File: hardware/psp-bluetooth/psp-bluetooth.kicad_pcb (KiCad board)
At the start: 2 copper layers, 45.7 x 73.7 mm, 16 parts, among them J1 Left Connector, J2 Center Connector, J3 Right Connector, J4 Analog Connector, J5 PSP Power out, J6 Power IN, J7 Serial, J8 Vin Toggle, P1 Digital, P2 Analog, P3 CONN_01X01, P4 CONN_01X01, P5 CONN_01X01, P6 CONN_01X01, U1 MCP4251-xxxx-P

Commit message: Final
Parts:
- added JP1: SJ Vin Toggle, Jumper:SolderJumper-2_P1.3mm_Open_Pad1.0x1.5mm, F.Cu at (148.0, 64.1)
- added SW1: SW_Push, Button_Switch_SMD:SW_Push_1P1T_NO_6x6mm_H9.5mm, F.Cu at (120.7, 92.7)
- J6: value Power IN -> Barrel_Jack; footprint Connector_PinHeader_2.54mm:PinHeader_1x02_P2.54mm_Vertical -> Connector_BarrelJack:BarrelJack_CUI_PJ-063AH_Horizontal
- moved J7 22.5 mm to (133.3, 71.1)
- moved J5 18.5 mm to (134.0, 64.1), turned to -90 degrees
- moved S1 6.54 mm to (142.9, 54.5)
- moved J6 4.28 mm to (125.1, 58.8), turned to 180 degrees
- moved J8 4.07 mm to (152.4, 64.1), turned to 90 degrees
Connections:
- net Net-(J4-Pad2) renamed /P1W
- net Net-(J4-Pad3) renamed /P0A/P1A
- net Net-(J4-Pad4) renamed /P0W
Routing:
- net /A6 (D20): track 0.00 -> 40.7 mm
- net /1(Tx): track 33.4 -> 6.15 mm
- net /0(Rx): track 33.4 -> 6.15 mm
- net Net-(J5-Pad2): track 22.3 -> 42.3 mm
- net VIN: track 7.86 -> 16.9 mm
- net Net-(J6-Pad2): track 8.17 -> 15.9 mm
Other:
- board text added: "+ -"
- board text added: "Arduino Nano 33 IOT"
- board text added: "Centre Connector"
- board text added: "Controller Sync"
- board text added: "Left Connector"
- board text added: "MCP4251"
- board text added: "PSP Bluetooth Consolizer V2.5 Stephen Cooper 2022"
- board text added: "Right Connector"
- board text added: "usb"
- board text removed: "GND"
- board text removed: "PSP Bluetooth Consolizer V2 Stephen Cooper 2022"
- board text removed: "Power"
- board text removed: "rx"
- board text removed: "tx"

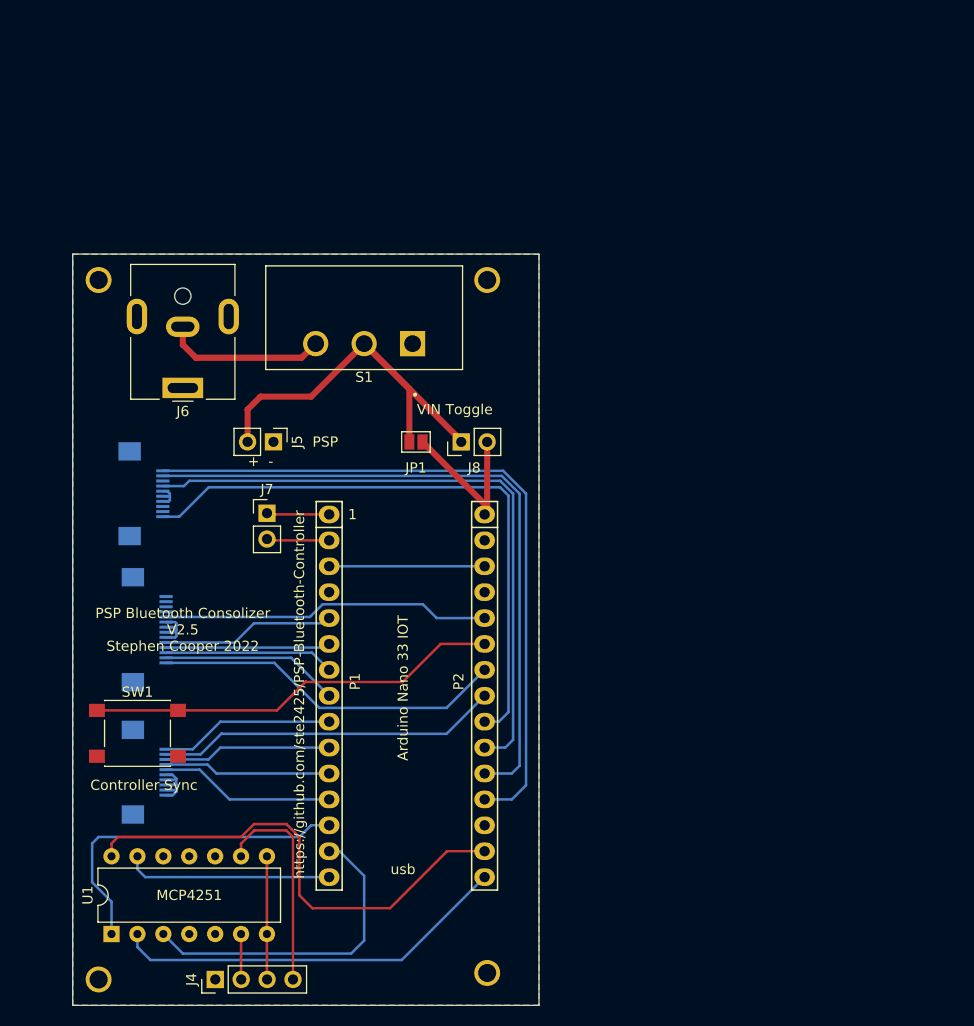
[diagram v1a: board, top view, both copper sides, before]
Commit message: Made kicad project portable and finished V1.
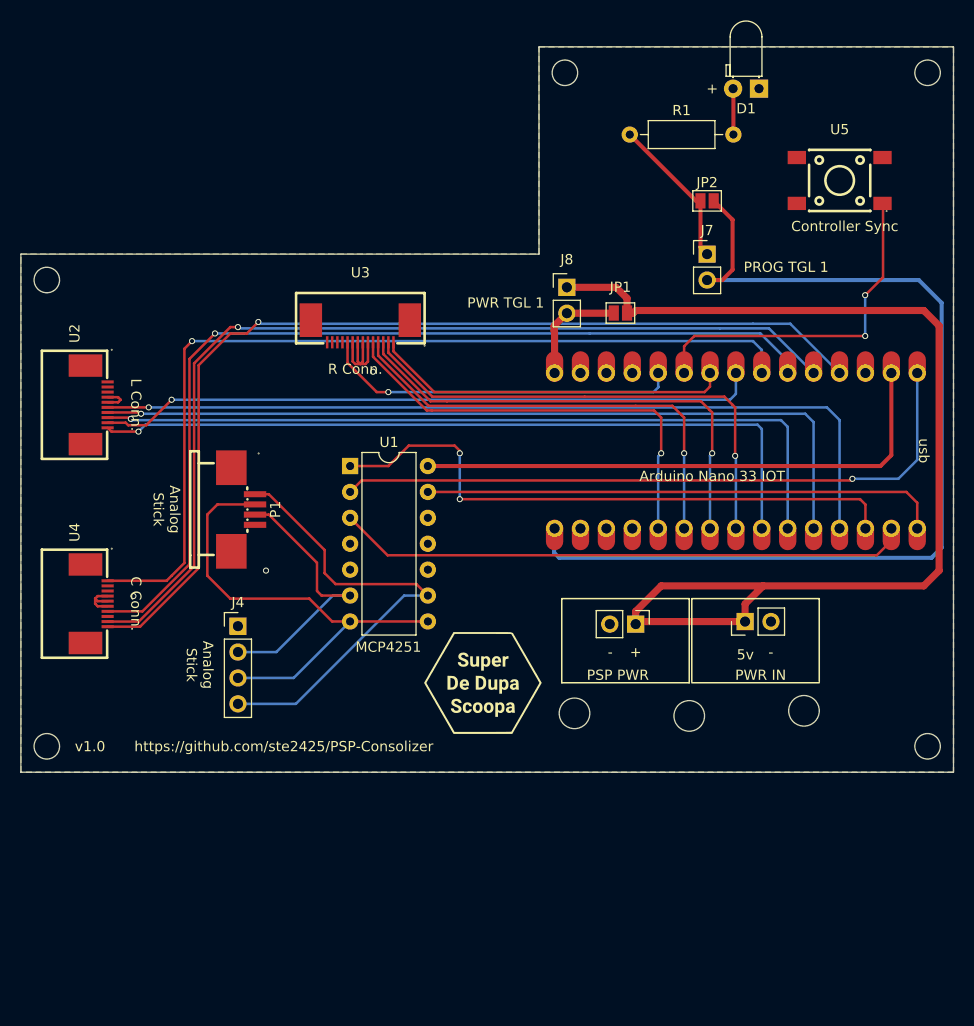
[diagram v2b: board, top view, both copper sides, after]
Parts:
- removed J5: PSP Power out, Connector_PinHeader_2.54mm:PinHeader_1x02_P2.54mm_Vertical
- removed J6: Barrel_Jack, Connector_BarrelJack:BarrelJack_CUI_PJ-063AH_Horizontal
- removed P2: Analog, Socket_Arduino_Nano:Socket_Strip_Arduino_1x15
- removed P3, P4, P5, P6: CONN_01X01, Socket_Arduino_Nano:1pin_Nano
- removed S1: L102021ML04Q, L102021ML04Q:SW_L102021ML04Q
- removed SW1: SW_Push, Button_Switch_SMD:SW_Push_1P1T_NO_6x6mm_H9.5mm
- added D1: LED, LED_THT:LED_D3.0mm_Horizontal_O1.27mm_Z6.0mm, F.Cu at (181.6, 29.5)
- added G***: LOGO, Graphics:pcblogo, F.Cu at (154.5, 87.8)
- added H1: MountingHole, MountingHole:MountingHole_2.5mm, F.Cu at (162.6, 27.9)
- added H2: MountingHole, MountingHole:MountingHole_2.5mm, F.Cu at (198.1, 27.9)
- added H3: MountingHole, MountingHole:MountingHole_2.5mm, F.Cu at (198.1, 94.0)
- added H4: MountingHole, MountingHole:MountingHole_2.5mm, F.Cu at (111.8, 94.0)
- added H5: MountingHole, MountingHole:MountingHole_2.5mm, F.Cu at (111.8, 48.3)
- added JP2: SJ LED Indicator, Jumper:SolderJumper-2_P1.3mm_Open_Pad1.0x1.5mm, F.Cu at (176.5, 40.5)
- added R1: 140 ohm, Resistor_THT:R_Axial_DIN0207_L6.3mm_D2.5mm_P10.16mm_Horizontal, F.Cu at (168.9, 34.0)
- added REF**: MountingHole_3mm, MountingHole:MountingHole_3mm, F.Cu at (174.8, 91.0)
- added REF**: MountingHole_3mm, MountingHole:MountingHole_3mm, F.Cu at (186.0, 90.5)
- added REF**: MountingHole_3mm, MountingHole:MountingHole_3mm, F.Cu at (163.5, 90.8)
- added U2: AFC07-S10ECA-00, JLCPCB_footprint:FPC-SMD_P0.50-10P_LCS-SJ-H2.0, F.Cu at (114.5, 60.5)
- added U3: AFC07-S14ECA-00, JLCPCB_footprint:FPC-SMD_P0.50-14P_LCS-SJ-H2.0, F.Cu at (142.5, 52.0)
- added U4: AFC07-S10ECA-00, JLCPCB_footprint:FPC-SMD_P0.50-10P_LCS-SJ-H2.0, F.Cu at (114.5, 80.0)
- added U5: TS-1102SD-A-F-R, JLCPCB_footprint:SW-SMD_4P-L6.0-W6.0-P4.50-LS9.2, F.Cu at (189.5, 38.5)
- J1: value Left Connector -> Arduino-NANO-33; footprint Connector_FFC-FPC:Hirose_FH12-10S-0.5SH_1x10-1MP_P0.50mm_Horizontal -> Nano_33:NANO_33_Socket_Castell&SMD; moved to F.Cu
- J2: value Center Connector -> Conn_01x02; footprint Connector_FFC-FPC:Hirose_FH12-10S-0.5SH_1x10-1MP_P0.50mm_Horizontal -> Connector_PinHeader_2.54mm:PinHeader_1x02_P2.54mm_Vertical; moved to F.Cu
- J3: value Right Connector -> Conn_01x02; footprint Connector_FFC-FPC:Hirose_FH12-14S-0.5SH_1x14-1MP_P0.50mm_Horizontal -> Connector_PinHeader_2.54mm:PinHeader_1x02_P2.54mm_Vertical; moved to F.Cu
- J7: value Serial -> Programming Header 1
- P1: value Digital -> FPC_4P_Pull_type_1_0MM_Under_the_next; footprint Socket_Arduino_Nano:Socket_Strip_Arduino_1x15 -> JLCPCB_footprint:FPC-SMD_AFA07-S04FCC-00
- moved J1 65.8 mm to (179.3, 65.0), turned to 180 degrees
- moved J3 58.6 mm to (180.2, 81.8)
- moved U1 51.5 mm to (141.5, 66.5), turned to 0 degrees
- moved J7 50.1 mm to (176.5, 45.7)
- moved J2 49.9 mm to (169.5, 82.0), turned to -90 degrees
- moved J4 34.7 mm to (130.5, 82.2), turned to 0 degrees
- moved JP1 23.7 mm to (168.0, 51.5), turned to 180 degrees
- moved J8 18.4 mm to (162.8, 49.0), turned to 0 degrees
- moved P1 10.5 mm to (129.0, 70.8)
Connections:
- J1 pad 1: GND -> /13(SCK)
- J1 pad 10: /6(**) -> /A6 (D20)
- J1 pad 2: GND -> +3V3
- J1 pad 3: GND -> unconnected-(J1-Pad3)
- J1 pad 4: GND -> /A0 (D14)
- J1 pad 5: GND -> /A1 (D15)
- J1 pad 6: /9(**) -> /A2 (D16)
- J1 pad 7: /8 -> /A3 (D17)
- J1 pad 8: /7 -> /A4 (D18)
- J1 pad 9: /A4 (D18) -> /A5 (D19)
- J2 pad 1: /A3 (D17) -> Net-(J8-Pad1)
- J2 pad 2: unconnected-(J2-Pad2) -> GND
- J3 pad 1: /A5 (D19) -> Net-(J8-Pad1)
- J3 pad 2: /5(**) -> GND
- J7 pad 1: /1(Tx) -> Net-(J7-Pad1)
- J7 pad 2: /0(Rx) -> /1(Tx)
- J8 pad 1: Net-(J5-Pad2) -> Net-(J8-Pad1)
- JP1 pad 1: Net-(J5-Pad2) -> Net-(J8-Pad1)
- P1 pad 1: /1(Tx) -> GND
- P1 pad 2: /0(Rx) -> /P1W
- P1 pad 3: /Reset -> /P0A/P1A
- P1 pad 4: GND -> /P0W
- P1 pad 5: /2 -> unconnected-(P1-Pad5)
- P1 pad 6: /3(**) -> unconnected-(P1-Pad6)
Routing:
- net Net-(J8-Pad1): track 0.00 -> 111.0 mm
- net /1(Tx): track 6.15 -> 99.4 mm
- net /9(**): track 17.2 -> 82.9 mm, vias 0 -> 1
- net /8: track 16.4 -> 80.0 mm, vias 0 -> 1
- net /7: track 16.5 -> 77.0 mm, vias 0 -> 1
- net /6(**): track 17.1 -> 74.5 mm, vias 0 -> 1
- net Net-(J5-Pad2): track 42.3 -> 0.00 mm
- net /P0A/P1A: track 12.1 -> 47.9 mm
- net /5(**): track 17.5 -> 49.1 mm, vias 0 -> 1
- net /A4 (D18): track 33.7 -> 65.0 mm, vias 0 -> 1
- net /12(MISO): track 20.4 -> 50.9 mm
- net /4: track 16.7 -> 47.2 mm, vias 0 -> 1
- net /A2 (D16): track 62.3 -> 92.1 mm, vias 0 -> 1
- net /A3 (D17): track 59.4 -> 88.8 mm, vias 0 -> 1
- net /A1 (D15): track 66.1 -> 94.7 mm, vias 0 -> 1
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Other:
- board size 45.7 x 73.7 mm -> 91.4 x 71.1 mm
- board text added: "+"
- board text added: "-"
- board text added: "5v"
- board text added: "Analog Stick"
- board text added: "C Conn."
- board text added: "Following FFC & Connector types [MUST] be used * Type A FFC & Top Interfacing Connector * Type D FFC & Bottom Interfacing Connector"
- board text added: "IMPORTANT"
- board text added: "L Conn."
- board text added: "PROG TGL 1"
- board text added: "PROG TGL 1 [MUST] be disconnected when programming"
- board text added: "PSP PWR"
- board text added: "PWR IN"
- board text added: "PWR TGL 1"
- board text added: "PWR TGL 1 [MUST] be disconnected when powered via USB"
- board text added: "R Conn."
- board text added: "https://github.com/ste2425/PSP-Consolizer"
- board text added: "v1.0"
- board text removed: "+ -"
- board text removed: "1"
- board text removed: "Centre Connector"
- board text removed: "Left Connector"
- board text removed: "PSP"
- board text removed: "PSP Bluetooth Consolizer V2.5 Stephen Cooper 2022"
- board text removed: "Right Connector"
- board text removed: "VIN Toggle"
- board text removed: "https://github.com/ste2425/PSP-Bluetooth-Controller"
